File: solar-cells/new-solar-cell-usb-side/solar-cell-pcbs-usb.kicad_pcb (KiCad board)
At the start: 2 copper layers, 80 x 103.5 mm, 21 parts, among them J1 Solar Cell

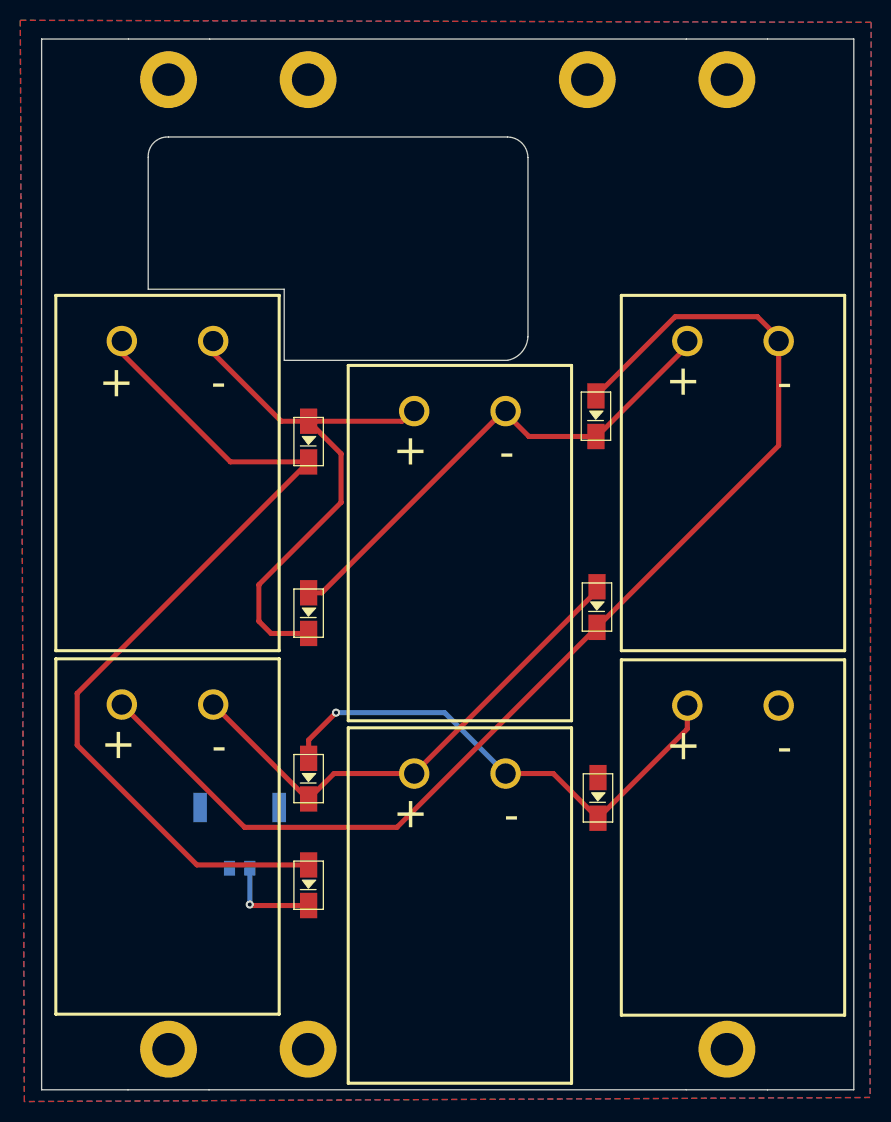
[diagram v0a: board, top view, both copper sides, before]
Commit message: fixing up usb side
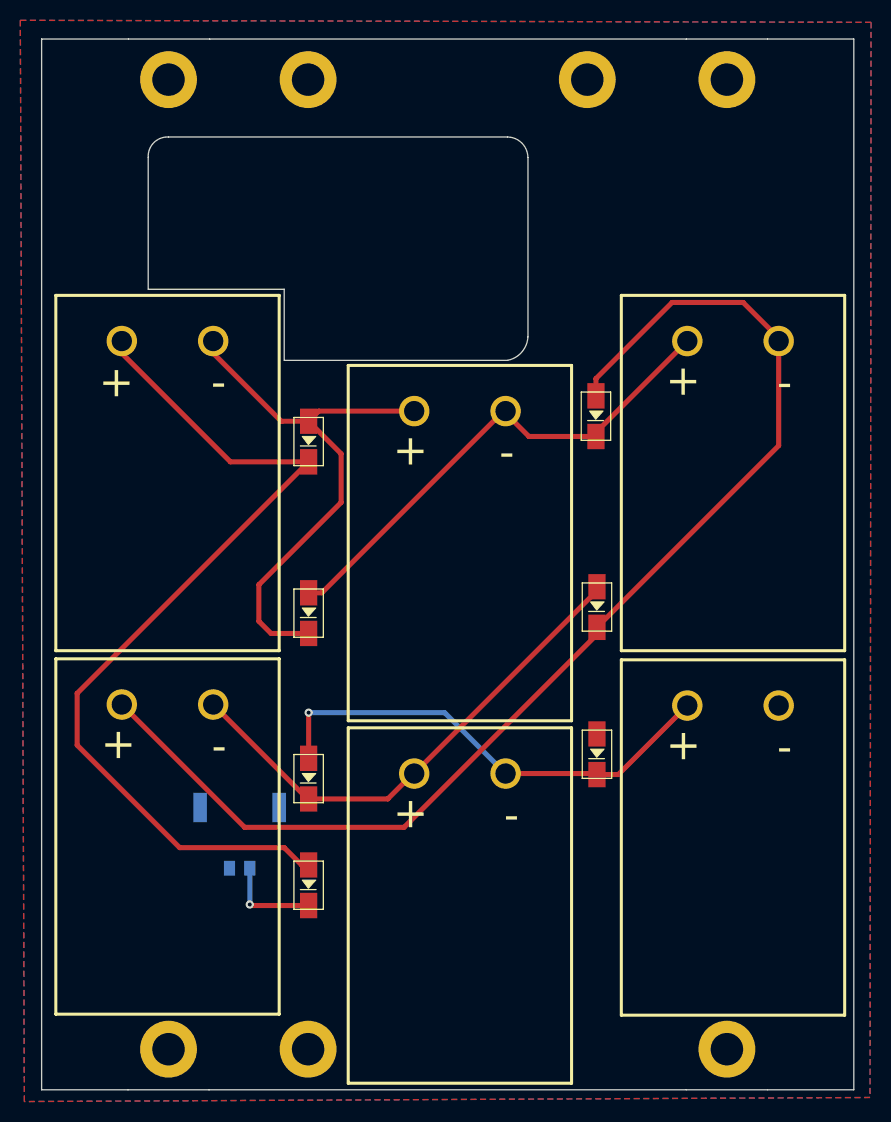
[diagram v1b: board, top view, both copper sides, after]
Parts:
- moved D6 4.30 mm to (126.8, 109.2)
- renumbered H8 to H7
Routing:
- net Net-(D5-Pad2): track 50.5 -> 47.5 mm
- net Net-(D3-Pad2): track 118.3 -> 120.8 mm
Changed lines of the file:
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@@
   (net 8 "VSOLAR")
   (footprint "ISP:DO-214AC" (layer "F.Cu")
-    (at 126.9 113.5 90)
+    (at 126.8 109.2 90)
     (property "Sheetfile" "solar-cell-pcbs-usb.kicad_sch")
     (property "Sheetname" "")
@@
     (property "Sheetname" "")
     (attr exclude_from_pos_files)
-    (fp_text reference "H8" (at 0 -3.8) (layer "F.Fab")
+    (fp_text reference "H7" (at 0 -3.8) (layer "F.Fab")
       (effects (font (size 1 1) (thickness 0.15)))
     )
@@
     (style (thickness 0.15) (arrow_length 1.27) (text_position_mode 0) (extension_height 0.58642) (extension_offset 0.5) keep_text_aligned)
   )
+  (segment (start 97.7 120.1) (end 98.4 120.1) (width 0.5) (layer "F.Cu") (net 2))
   (segment (start 75.6 103.2) (end 75.6 108.3) (width 0.5) (layer "F.Cu") (net 2))
-  (segment (start 75.6 108.3) (end 87.4 120.1) (width 0.5) (layer "F.Cu") (net 2))
+  (segment (start 75.6 108.3) (end 85.7 118.4) (width 0.5) (layer "F.Cu") (net 2))
   (segment (start 90.7 80.4) (end 98.4 80.4) (width 0.5) (layer "F.Cu") (net 2))
+  (segment (start 85.7 118.4) (end 96 118.4) (width 0.5) (layer "F.Cu") (net 2))
+  (segment (start 96 118.4) (end 97.7 120.1) (width 0.5) (layer "F.Cu") (net 2))
   (segment (start 80 69.7) (end 90.7 80.4) (width 0.5) (layer "F.Cu") (net 2))
   (segment (start 98.4 80.4) (end 75.6 103.2) (width 0.5) (layer "F.Cu") (net 2))
-  (segment (start 87.4 120.1) (end 98.4 120.1) (width 0.5) (layer "F.Cu") (net 2))
   (segment (start 80 68.5) (end 80 69.7) (width 0.5) (layer "F.Cu") (net 2))
   (segment (start 101.6 79.6) (end 101.6 84.4) (width 0.5) (layer "F.Cu") (net 3))
   (segment (start 95.7 76.4) (end 98.4 76.4) (width 0.5) (layer "F.Cu") (net 3))
-  (segment (start 108.6 75.4) (end 107.6 76.4) (width 0.5) (layer "F.Cu") (net 3))
   (segment (start 89 68.5) (end 89 69.7) (width 0.5) (layer "F.Cu") (net 3))
   (segment (start 89 69.7) (end 95.7 76.4) (width 0.5) (layer "F.Cu") (net 3))
@@
   (segment (start 94.7 97.3) (end 98.4 97.3) (width 0.5) (layer "F.Cu") (net 3))
   (segment (start 101.6 84.4) (end 93.5 92.5) (width 0.5) (layer "F.Cu") (net 3))
-  (segment (start 107.6 76.4) (end 98.4 76.4) (width 0.5) (layer "F.Cu") (net 3))
+  (segment (start 99.4 75.4) (end 98.4 76.4) (width 0.5) (layer "F.Cu") (net 3))
   (segment (start 98.4 76.4) (end 101.6 79.6) (width 0.5) (layer "F.Cu") (net 3))
+  (segment (start 108.6 75.4) (end 99.4 75.4) (width 0.5) (layer "F.Cu") (net 3))
   (segment (start 117.6 75.4) (end 120.1 77.9) (width 0.5) (layer "F.Cu") (net 4))
+  (segment (start 126.7 77.9) (end 126.7 77.5) (width 0.5) (layer "F.Cu") (net 4))
   (segment (start 120.1 77.9) (end 126.7 77.9) (width 0.5) (layer "F.Cu") (net 4))
   (segment (start 98.4 93.3) (end 99.7 93.3) (width 0.5) (layer "F.Cu") (net 4))
-  (segment (start 126.8 77.9) (end 136.1 68.6) (width 0.5) (layer "F.Cu") (net 4))
+  (segment (start 126.7 77.5) (end 135.7 68.5) (width 0.5) (layer "F.Cu") (net 4))
   (segment (start 99.7 93.3) (end 117.6 75.4) (width 0.5) (layer "F.Cu") (net 4))
-  (segment (start 126.7 77.9) (end 126.8 77.9) (width 0.5) (layer "F.Cu") (net 4))
+  (segment (start 136 68.5) (end 136.1 68.6) (width 0.5) (layer "F.Cu") (net 4))
   (segment (start 144.7 68.5) (end 144.7 78.8) (width 0.5) (layer "F.Cu") (net 5))
+  (segment (start 107.8 116.4) (end 126.8 97.4) (width 0.5) (layer "F.Cu") (net 5))
   (segment (start 80 104.3) (end 92.1 116.4) (width 0.5) (layer "F.Cu") (net 5))
-  (segment (start 92.1 116.4) (end 107.1 116.4) (width 0.5) (layer "F.Cu") (net 5))
-  (segment (start 142.6 66.1) (end 145.1 68.6) (width 0.5) (layer "F.Cu") (net 5))
-  (segment (start 126.7 73.9) (end 134.5 66.1) (width 0.5) (layer "F.Cu") (net 5))
-  (segment (start 107.1 116.4) (end 126.8 96.7) (width 0.5) (layer "F.Cu") (net 5))
-  (segment (start 134.5 66.1) (end 142.6 66.1) (width 0.5) (layer "F.Cu") (net 5))
+  (segment (start 141.2 64.7) (end 145.1 68.6) (width 0.5) (layer "F.Cu") (net 5))
   (segment (start 144.7 78.8) (end 126.8 96.7) (width 0.5) (layer "F.Cu") (net 5))
+  (segment (start 126.7 72.2) (end 134.2 64.7) (width 0.5) (layer "F.Cu") (net 5))
+  (segment (start 126.8 97.4) (end 126.8 96.7) (width 0.5) (layer "F.Cu") (net 5))
+  (segment (start 126.7 73.9) (end 126.7 72.2) (width 0.5) (layer "F.Cu") (net 5))
+  (segment (start 92.1 116.4) (end 107.8 116.4) (width 0.5) (layer "F.Cu") (net 5))
+  (segment (start 134.2 64.7) (end 141.2 64.7) (width 0.5) (layer "F.Cu") (net 5))
   (segment (start 126.8 93.1) (end 126.8 92.7) (width 0.25) (layer "F.Cu") (net 6))
-  (segment (start 100.9 111.1) (end 98.4 113.6) (width 0.5) (layer "F.Cu") (net 6))
+  (segment (start 108.7 111.1) (end 106.2 113.6) (width 0.5) (layer "F.Cu") (net 6))
   (segment (start 98.4 113.6) (end 98.3 113.6) (width 0.25) (layer "F.Cu") (net 6))
-  (segment (start 108.8 111.1) (end 100.9 111.1) (width 0.5) (layer "F.Cu") (net 6))
+  (segment (start 106.2 113.6) (end 98.4 113.6) (width 0.5) (layer "F.Cu") (net 6))
   (segment (start 108.8 111.1) (end 126.8 93.1) (width 0.5) (layer "F.Cu") (net 6))
   (segment (start 98.3 113.6) (end 89 104.3) (width 0.5) (layer "F.Cu") (net 6))
-  (segment (start 122.5 111.1) (end 126.9 115.5) (width 0.5) (layer "F.Cu") (net 7))
-  (segment (start 117.8 111.1) (end 122.5 111.1) (width 0.5) (layer "F.Cu") (net 7))
-  (segment (start 135.7 106.7) (end 135.7 104.4) (width 0.5) (layer "F.Cu") (net 7))
-  (segment (start 98.4 107.8) (end 101.1 105.1) (width 0.5) (layer "F.Cu") (net 7))
-  (segment (start 98.4 109.6) (end 98.4 107.8) (width 0.5) (layer "F.Cu") (net 7))
-  (segment (start 126.9 115.5) (end 135.7 106.7) (width 0.5) (layer "F.Cu") (net 7))
-  (via (at 101.1 105.1) (size 0.8) (drill 0.4) (layers "F.Cu" "B.Cu") (free) (net 7))
-  (segment (start 101.1 105.1) (end 111.8 105.1) (width 0.5) (layer "B.Cu") (net 7))
+  (segment (start 108.8 111.1) (end 108.7 111.1) (width 0.5) (layer "F.Cu") (net 6))
+  (segment (start 135.3 104.4) (end 135.7 104.4) (width 0.5) (layer "F.Cu") (net 7))
+  (segment (start 98.4 105.1) (end 98.4 109.6) (width 0.5) (layer "F.Cu") (net 7))
+  (segment (start 135.7 104.4) (end 128.9 111.2) (width 0.5) (layer "F.Cu") (net 7))
+  (segment (start 126.6 111.1) (end 126.7 111.2) (width 0.5) (layer "F.Cu") (net 7))
+  (segment (start 128.9 111.2) (end 126.7 111.2) (width 0.5) (layer "F.Cu") (net 7))
+  (segment (start 117.8 111.1) (end 126.6 111.1) (width 0.5) (layer "F.Cu") (net 7))
+  (via (at 98.4 105.1) (size 0.8) (drill 0.4) (layers "F.Cu" "B.Cu") (free) (net 7))
+  (segment (start 98.4 105.1) (end 111.8 105.1) (width 0.5) (layer "B.Cu") (net 7))
   (segment (start 111.8 105.1) (end 117.8 111.1) (width 0.5) (layer "B.Cu") (net 7))
   (segment (start 92.7 124.1) (end 98.4 124.1) (width 0.5) (layer "F.Cu") (net 8))

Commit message: made solar cells 3s2p config
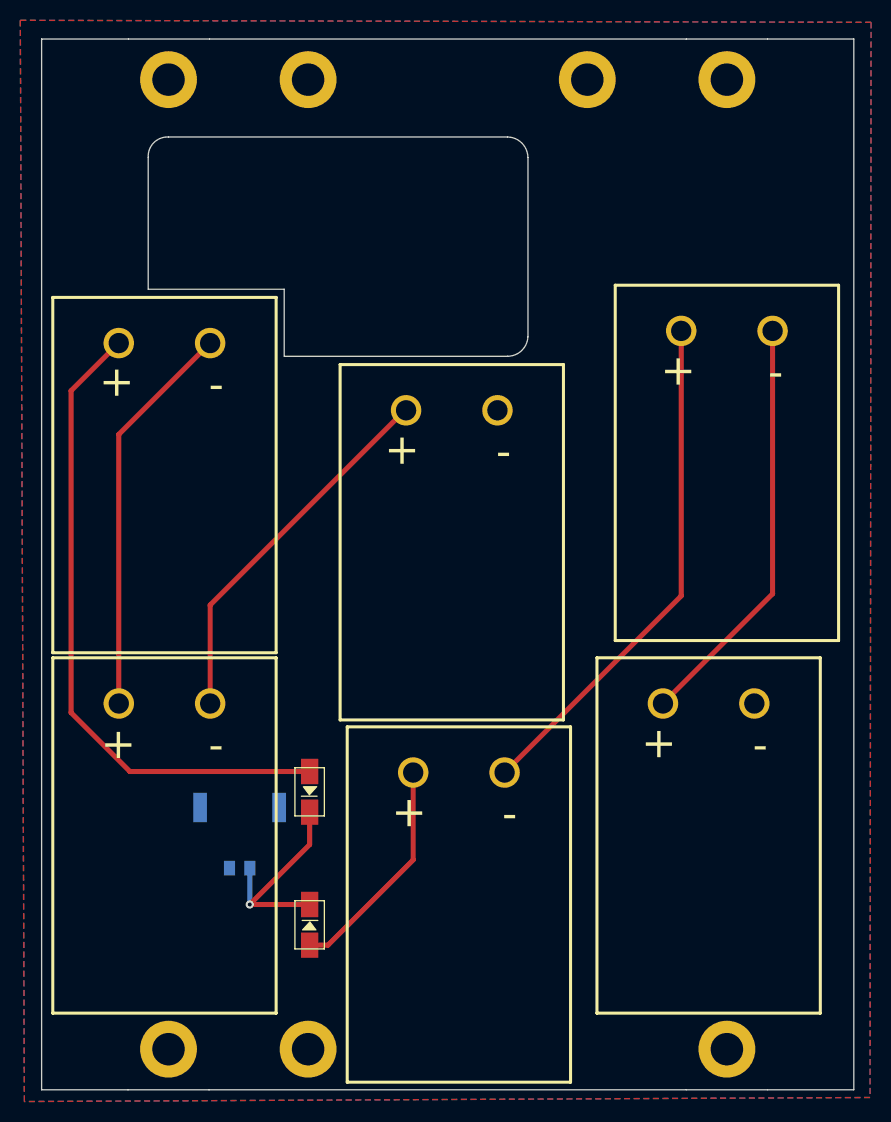
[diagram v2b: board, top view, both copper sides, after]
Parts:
- removed D3, D4, D5, D6, D9: CDBA240LL-HF, ISP:DO-214AC
- moved SC1 51.3 mm to (113.7, 124.0)
- moved D1 47.6 mm to (98.5, 126.0), turned to -90 degrees
- moved SC6 40.2 mm to (113.0, 88.3)
- moved SC3 35.8 mm to (138.3, 117.2)
- moved SC4 35.6 mm to (84.7, 81.7)
- moved SC5 29.9 mm to (84.7, 117.2)
- moved SC2 27.5 mm to (140.1, 80.5)
- moved D2 17.6 mm to (98.5, 112.9)
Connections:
- D1 pad 1: Net-(D1-Pad1) -> VSOLAR
- D2 pad 1: Net-(D1-Pad2) -> VSOLAR
- SC1 pad 1: Net-(D1-Pad1) -> Net-(D1-Pad2)
- SC1 pad 2: Net-(D1-Pad2) -> Net-(SC1-Pad2)
- SC2 pad 1: Net-(D1-Pad2) -> Net-(SC1-Pad2)
- SC2 pad 2: Net-(D2-Pad2) -> Net-(SC2-Pad2)
- SC3 pad 1: Net-(D2-Pad2) -> Net-(SC2-Pad2)
- SC3 pad 2: Net-(D3-Pad2) -> GND
- SC4 pad 1: Net-(D3-Pad2) -> Net-(D2-Pad2)
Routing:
- net Net-(D3-Pad2): track 120.8 -> 0.00 mm
- net Net-(D1-Pad1): track 89.1 -> 0.00 mm
- net Net-(SC1-Pad2): track 0.00 -> 50.7 mm
- net Net-(SC2-Pad2): track 0.00 -> 41.2 mm
- net Net-(D1-Pad2): track 53.8 -> 22.3 mm
- net Net-(D2-Pad2): track 50.0 -> 64.2 mm
- net VSOLAR: track 9.42 -> 21.2 mm
- net Net-(SC4-Pad2): track 50.5 -> 39.2 mm
- net Net-(SC5-Pad2): track 47.5 -> 36.9 mm, vias 1 -> 0
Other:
- outline, holes or cut-outs redrawn
